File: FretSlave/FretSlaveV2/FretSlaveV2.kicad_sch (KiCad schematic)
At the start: 17 parts, among them J1 ISCP, J2 Frets1-4, J3 Frets5-8, J4 Frets9-12, J5 Frets13-15, SW1 Reset, U1 PIC16F1788

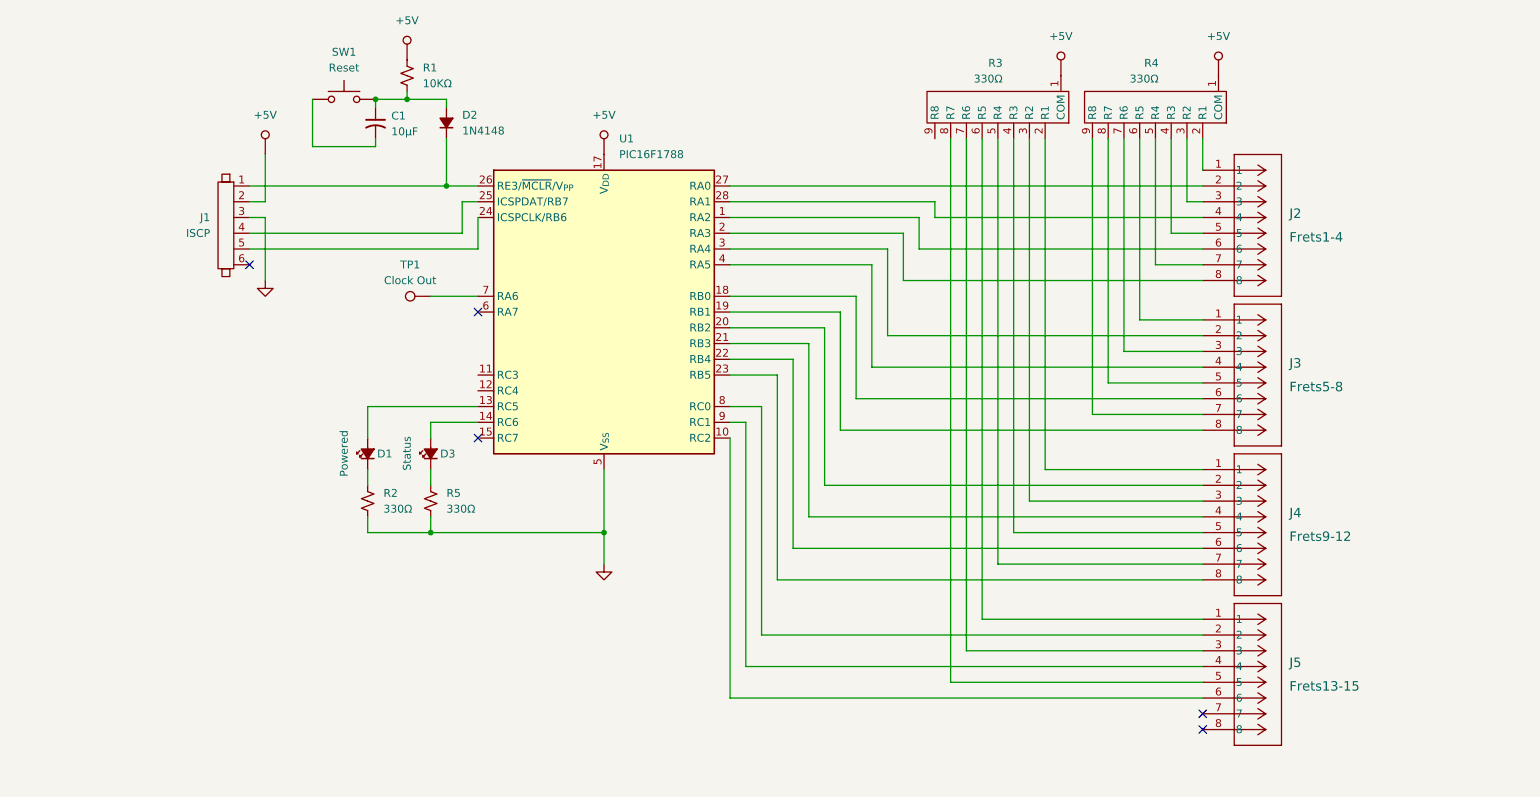
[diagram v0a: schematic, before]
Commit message: decided on utilizing a universal setup for the slave board
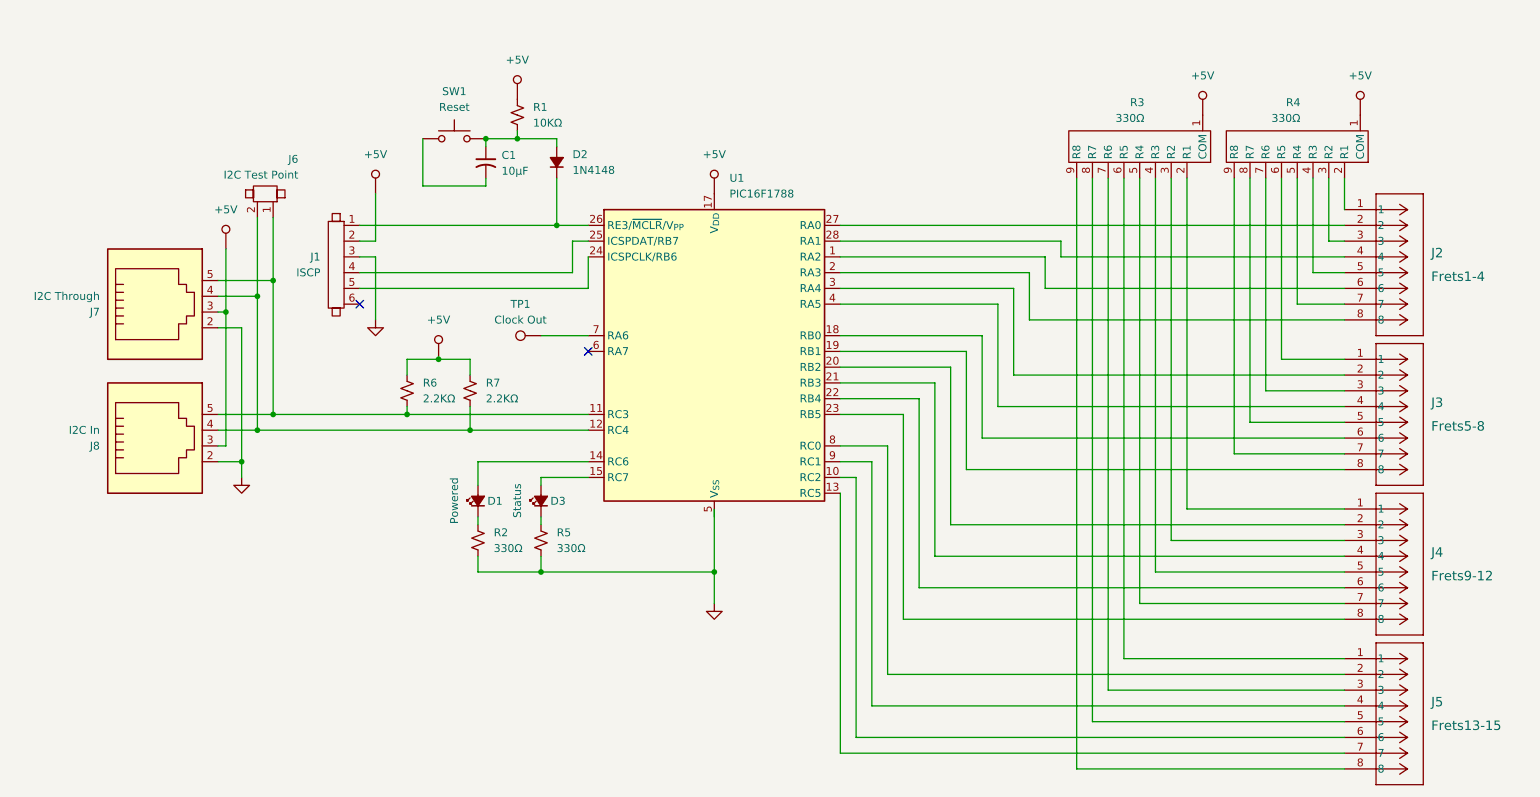
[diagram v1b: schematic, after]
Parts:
- added J6: I2C Test Point, 2JB_Footprints:1X2_100mil_Header, symbol 2_JB_Custom_sym:Jumper_2_Pin
- added J7: I2C Through, 2JB_Footprints:RJ11, symbol Connector:RJ11
- added J8: I2C In, 2JB_Footprints:RJ11, symbol Connector:RJ11
- added R6, R7: 2.2KΩ, 2JB_Footprints:C_0805, symbol Device:R_Small_US
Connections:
- net GND: now also J7.2, J8.2; no longer U1.16 (V_{SS}), U1.5 (V_{SS})
- net at J5.7: now also U1.13 (RC5)
- net at J5.8: now also R3.9 (R8)
- net at D3.2 (A): now also U1.15 (RC7); no longer U1.14 (RC6)
- net at U1.11 (RC3): now also J6.1, J7.5, J8.5, R6.2
- net at U1.12 (RC4): now also J6.2, J7.4, J8.4, R7.2
- net at D1.2 (A): now also U1.14 (RC6); no longer U1.13 (RC5)
- new net: J7.3, J8.3
- new net: R6.1, R7.1
- new net: U1.16 (V_{SS}), U1.5 (V_{SS})
- no-connect marks 5 -> 2
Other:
- moved on the sheet: C1, D1, D2, D3, J1, J2, J3, J4, J5, R1, R2, R3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
